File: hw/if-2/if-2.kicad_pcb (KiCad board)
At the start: 4 copper layers, 100 x 130 mm, 198 parts, among them J1 DB25_Socket, J2 PJ-102AH, J3 Conn_02x12_Odd_Even, J4 Conn_01x02, J5 Conn_01x02, Q1 MMBT3904, Q11 MMBT3904, Q12 MMBT3904, Q2 MMBT3904, U10 NCP1117-5.0_SOT223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

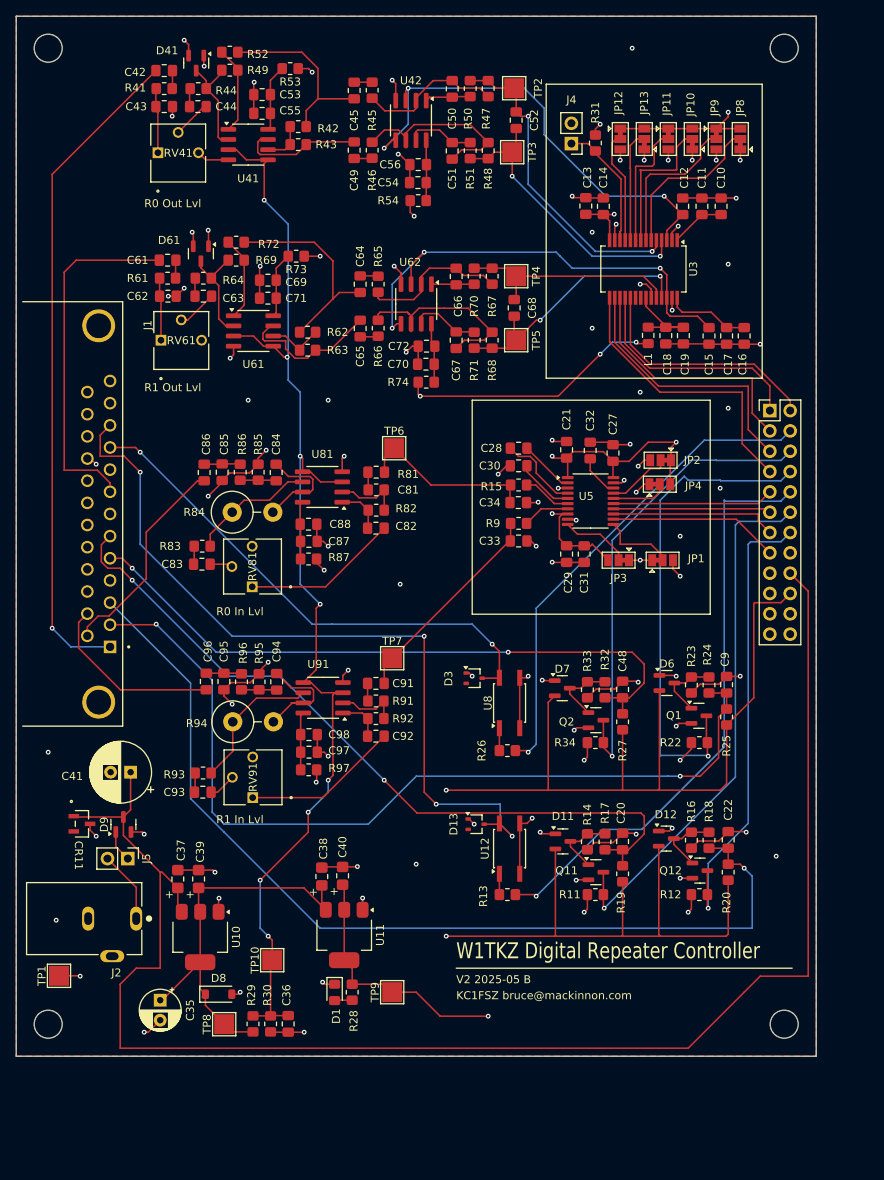
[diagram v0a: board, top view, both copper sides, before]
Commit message: (Pre fab) Resolved warning with DB25 shell connections to ground
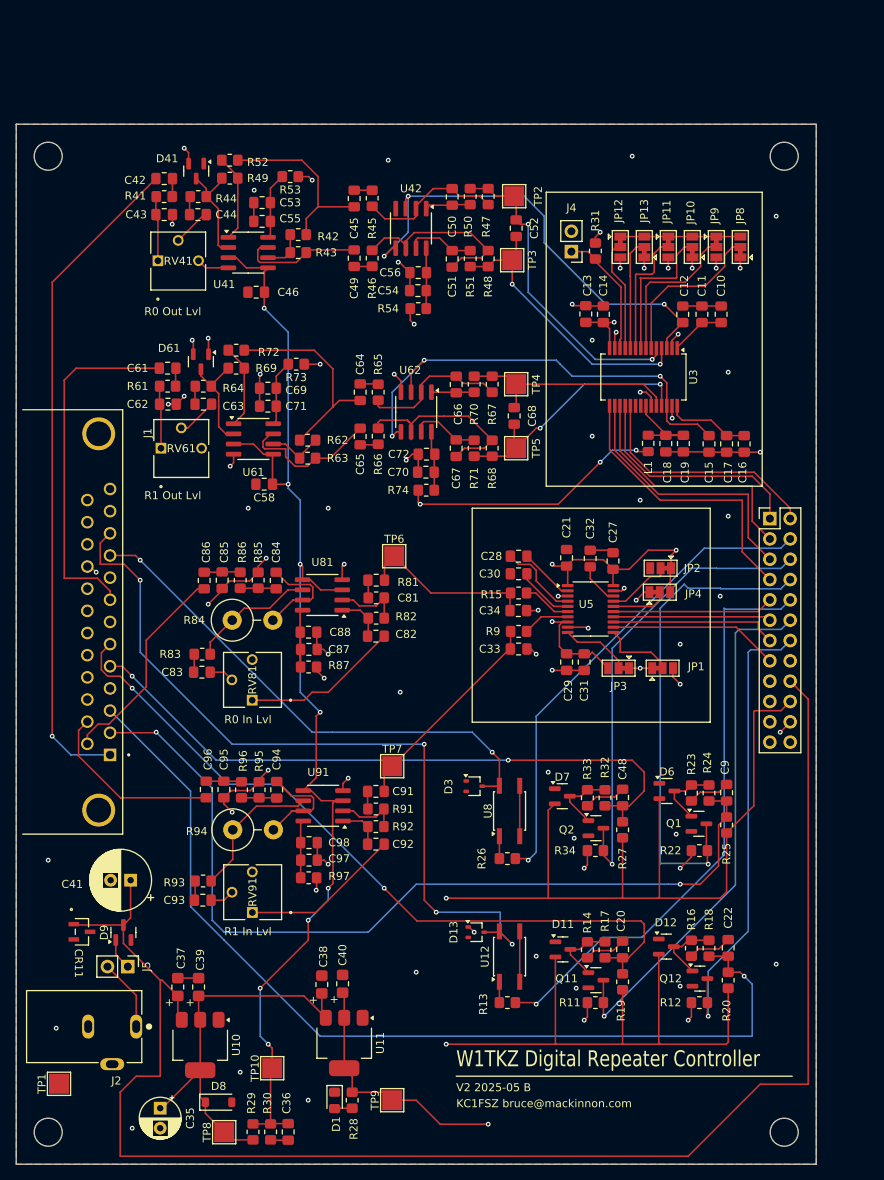
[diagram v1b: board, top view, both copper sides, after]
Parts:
- added C46: 1u, Capacitor_SMD:C_0805_2012Metric_Pad1.18x1.45mm_HandSolder, F.Cu at (69.0, 52.5)
- added C58: 1u, Capacitor_SMD:C_0805_2012Metric_Pad1.18x1.45mm_HandSolder, F.Cu at (70.0, 76.5)
- moved RV91 14.4 mm to (68.5, 130.0)
- moved RV81 14.2 mm to (68.5, 103.5)
- moved D12 13.5 mm to (120.3, 134.3)
- moved J5 13.5 mm to (53.0, 136.8)
- moved Q12 13.5 mm to (124.5, 138.3)
- moved R11 13.5 mm to (111.4, 141.3)
- moved R12 13.5 mm to (124.4, 141.3)
- moved R13 13.5 mm to (100.4, 141.3)
- moved U12 13.5 mm to (100.7, 135.6)
- moved C15 13.5 mm to (125.6, 71.5)
- moved C16 13.5 mm to (130.0, 71.5)
- moved C17 13.5 mm to (127.8, 71.5)
- moved C68 13.5 mm to (101.2, 68.0)
- moved L1 13.5 mm to (118.0, 71.4)
- moved C10 13.5 mm to (127.1, 55.3)
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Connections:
- J1 pad SH1: (no net) -> GND
- J1 pad SH2: (no net) -> GND
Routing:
- net GND: track 232.0 -> 166.5 mm, vias 83 -> 60
- net +3.3V: track 108.0 -> 103.8 mm, vias 17 -> 18
- net VBIAS: track 146.0 -> 149.4 mm

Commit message: (Pre fab) Added fill on bottom layer
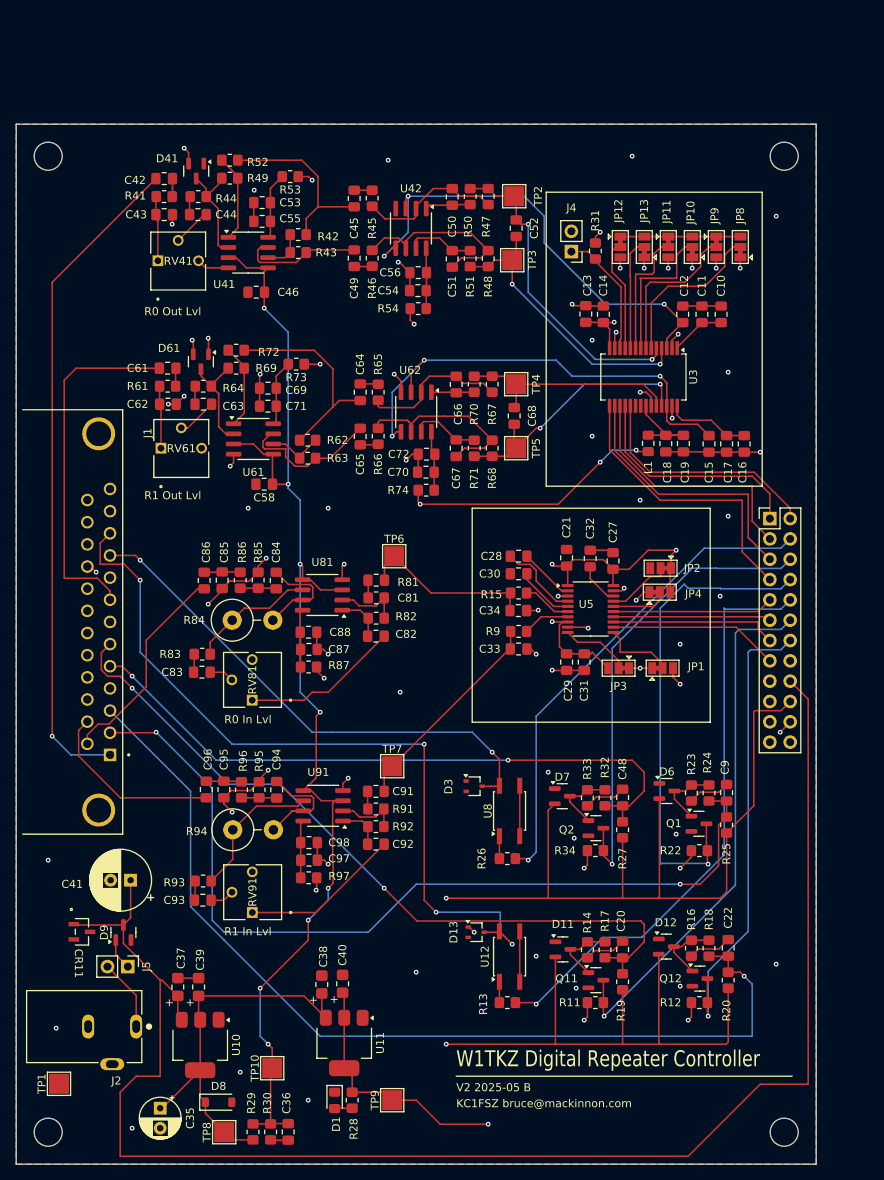
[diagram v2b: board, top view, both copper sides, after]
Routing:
- added copper zone on B.Cu, net GND
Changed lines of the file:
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@@
+		(net 2)
+		(net_name "GND")
+		(layer "B.Cu")
+		(hatch edge 0.5)
+		(priority 4)
+		(connect_pads
+			(clearance 0.5)
+		)
+		(min_thickness 0.25)
+		(filled_areas_thickness no)
+		(fill yes
+			(thermal_gap 0.5)
+			(thermal_bridge_width 0.5)
+		)
+		(polygon
+			(pts
+				(xy 39 31.5) (xy 39 161.5) (xy 139 161.5) (xy 139 31.5)
+			)
+		)
+	)
+	(zone
 		(net 2)
 		(net_name "GND")
